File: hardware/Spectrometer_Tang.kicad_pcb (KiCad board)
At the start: 2 copper layers, 75 x 57.5 mm, 62 parts, among them J1 USB_C_Receptacle_USB2.0, J2 Conn_01x08_Male, U1 Lichee_Tang, U2 FT245RQ, U3 TCD1500C, U4 AD8475xRMZ, U5 TXB0104PW, U6 ST662AB, U7 XC6206P302MR, U8 LTC2227

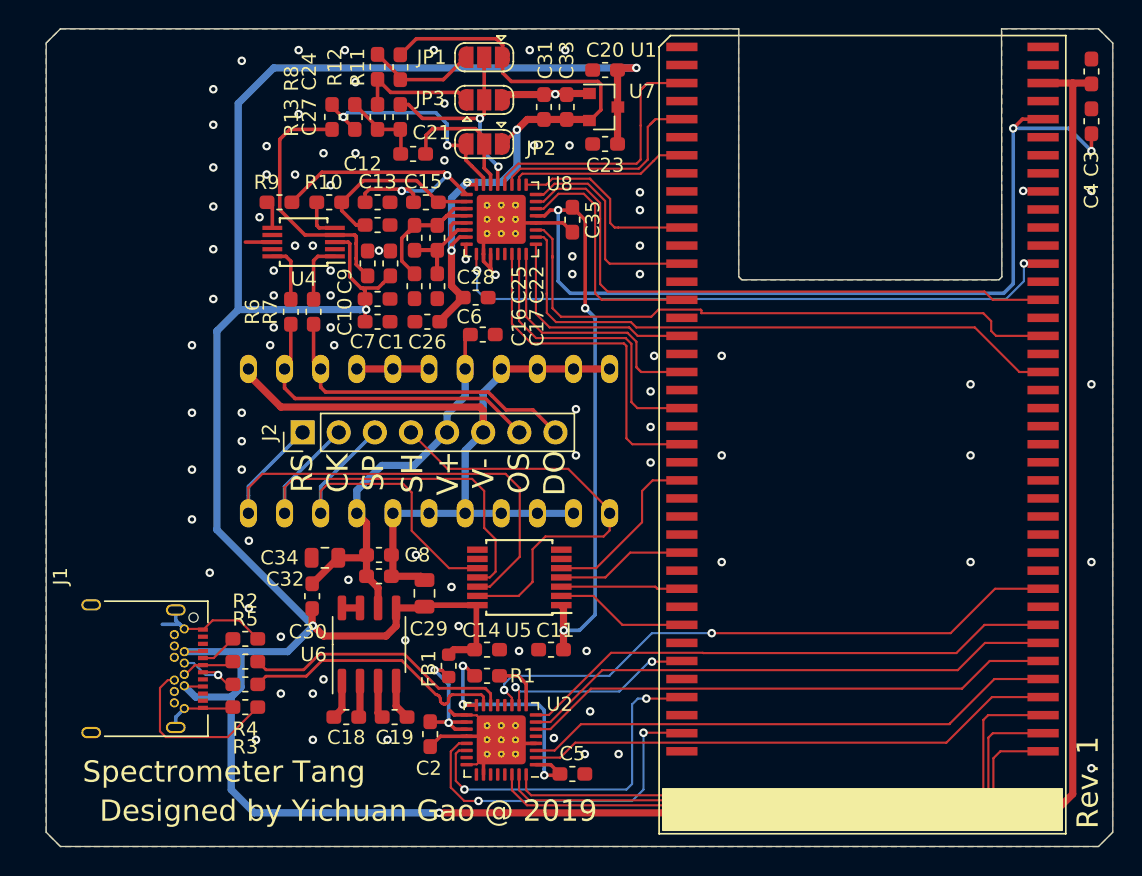
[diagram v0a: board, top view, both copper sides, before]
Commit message: Fix level converter & usb port location
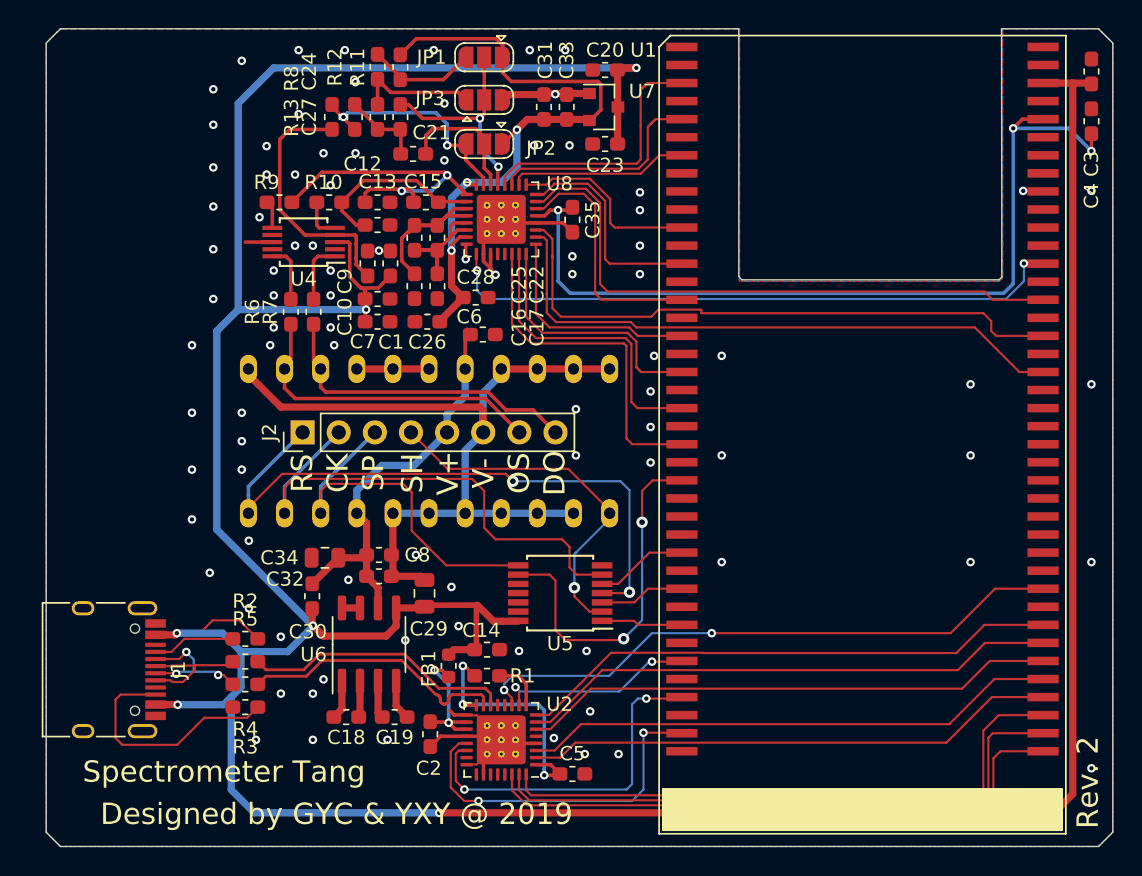
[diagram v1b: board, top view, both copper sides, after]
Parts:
- removed C11: 100nF, Capacitor_SMD:C_0603_1608Metric_Pad1.05x0.95mm_HandSolder
- J1: footprint Connector_USB:USB_C_Receptacle_Amphenol_12401548E4-2A -> Connector_USB:USB_C_Receptacle_HRO_TYPE-C-31-M-12
- U5: value TXB0104PW -> 74HC04
- moved U5 3.07 mm to (131.1, 67.2)
- moved J1 2.36 mm to (98.6, 72.6)
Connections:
- J1 pad A8: Net-(J1-PadA8) -> (no net)
- J1 pad B8: Net-(J1-PadB8) -> (no net)
- U1 pad 1: Net-(U1-Pad1) -> (no net)
- U1 pad 52: Net-(U1-Pad52) -> (no net)
- U1 pad 56: Net-(U1-Pad56) -> (no net)
- U1 pad 58: Net-(U1-Pad58) -> (no net)
- U1 pad 60: Net-(U1-Pad60) -> (no net)
- U1 pad 70: Net-(U1-Pad70) -> (no net)
- U1 pad 74: Net-(U1-Pad74) -> (no net)
- U2 pad 27: Net-(U2-Pad27) -> (no net)
- U2 pad 28: Net-(U2-Pad28) -> (no net)
- U4 pad 2: Net-(U4-Pad2) -> (no net)
- U4 pad 7: Net-(U4-Pad7) -> (no net)
- U4 pad 9: Net-(U4-Pad9) -> (no net)
- U5 pad 1: +3V3 -> /SH
- U5 pad 10: /CCD_SP -> (no net)
- U5 pad 11: /CCD_CLK -> (no net)
- U5 pad 12: /CCD_RS -> (no net)
- U5 pad 13: /CCD_SH -> (no net)
- U5 pad 2: /SH -> /CCD_SH
- U5 pad 4: /CLK -> /CCD_RS
- U5 pad 5: /SP -> /CLK
- U5 pad 6: Net-(U5-Pad6) -> /CCD_CLK
- U5 pad 8: Net-(U5-Pad8) -> /CCD_SP
- U5 pad 9: Net-(U5-Pad9) -> /SP
- U8 pad 12: Net-(U8-Pad12) -> (no net)
- U8 pad 13: Net-(U8-Pad13) -> (no net)
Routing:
- net +3V3: track 97.3 -> 61.3 mm, vias 5 -> 3
- net /SP: track 12.3 -> 25.4 mm, vias 0 -> 2
- net Earth: track 122.0 -> 112.5 mm
- net /CCD_RS: track 37.6 -> 45.1 mm, vias 0 -> 2
- net /CCD_CLK: track 31.2 -> 36.8 mm
- net Net-(J1-PadB5): track 12.2 -> 17.2 mm
- net /USB_P: track 3.79 -> 8.60 mm
- net +5V: track 254.1 -> 258.8 mm, vias 4 -> 6
- net /USB_N: track 5.26 -> 9.76 mm, vias 1 -> 3
- net /CCD_SH: track 30.2 -> 25.8 mm, vias 0 -> 1
- net /SH: track 9.32 -> 5.73 mm
- net Net-(J1-PadA5): track 2.66 -> 5.58 mm
- net /CCD_SP: track 24.1 -> 26.9 mm
- net /CLK: track 9.20 -> 6.52 mm
- net /RS: track 8.54 -> 6.01 mm
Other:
- board text added: "Designed by GYC & YXY @ 2019"
- board text added: "Rev. 2"
- board text removed: "Designed by Yichuan Gao @ 2019"
- board text removed: "Rev. 1"
